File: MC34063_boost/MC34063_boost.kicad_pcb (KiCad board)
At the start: 2 copper layers, 88.6 x 24 mm, 24 parts, among them J1 INPUT, J2 OUTPUT, Q1 2N2222, U1 MC34063AP

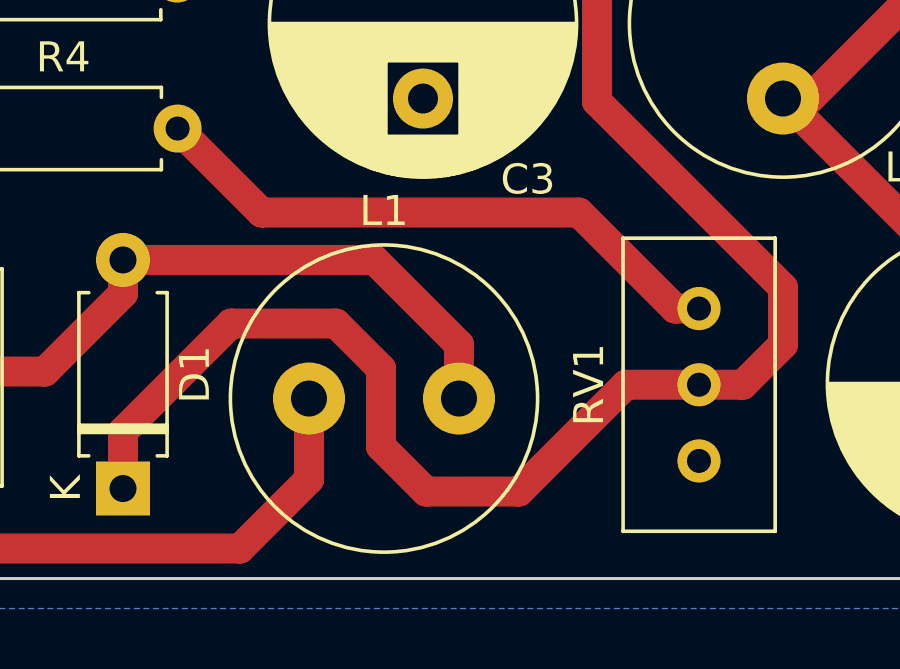
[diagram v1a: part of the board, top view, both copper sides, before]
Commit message: Made buck & inverter PCB's smaller for panelization
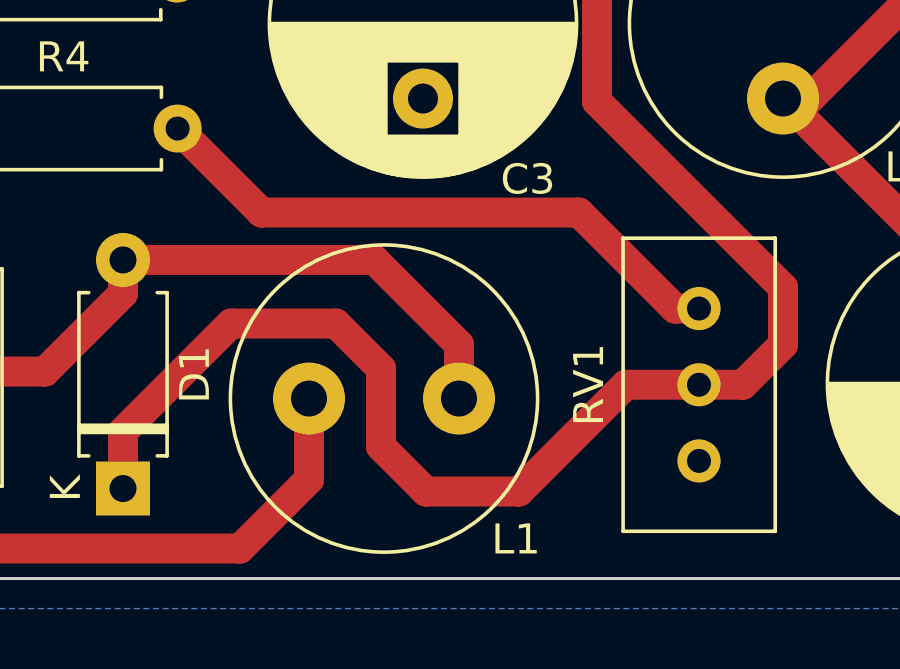
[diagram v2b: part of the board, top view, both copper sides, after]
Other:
- board text added: "https://github.com/DarioIriberri/MC34063_Converters"
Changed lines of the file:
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@@
   (general
     (thickness 1.6)
-    (drawings 13)
+    (drawings 14)
     (tracks 95)
     (zones 0)
@@
     (descr "Inductor, Radial series, Radial, pin pitch=5.00mm, , diameter=10.0mm, Neosid, SD12k, style3, http://www.neosid.de/produktblaetter/neosid_Festinduktivitaet_Sd12k.pdf")
     (tags "Inductor Radial series Radial pin pitch 5.00mm  diameter 10.0mm Neosid SD12k style3")
-    (fp_text reference L1 (at 2.5 -6.25) (layer F.SilkS)
+    (fp_text reference L1 (at 6.9 4.7) (layer F.SilkS)
       (effects (font (size 1 1) (thickness 0.15)))
     )
@@
     )
   )
+  (gr_text https://github.com/DarioIriberri/MC34063_Converters (at 104.1 81.5) (layer B.SilkS)
+    (effects (font (size 1.2 1.2) (thickness 0.15)) (justify mirror))
+  )
   (gr_text - (at 55.2 63.6 90) (layer F.SilkS)
     (effects (font (size 1.5 1.5) (thickness 0.3)))
@@
   (gr_line (start 45 83) (end 45 59) (layer Edge.Cuts) (width 0.1))
   (gr_line (start 133.6 83) (end 45 83) (layer Edge.Cuts) (width 0.1))
-  (segment (start 56.48 70.52) (end 59.98 70.52) (width 1) (layer F.Cu) (net 1))
   (segment (start 53.8 73.2) (end 56.48 70.52) (width 1) (layer F.Cu) (net 1))
   (segment (start 56.48 64.86) (end 58.34 63) (width 1) (layer F.Cu) (net 1))
@@
   (segment (start 52.5 68.7) (end 54.66 68.7) (width 1) (layer F.Cu) (net 1))
   (segment (start 53.5 73.5) (end 53.8 73.2) (width 1) (layer F.Cu) (net 1))
+  (segment (start 56.48 70.52) (end 59.98 70.52) (width 1) (layer F.Cu) (net 1))
   (segment (start 53.5 74.8) (end 53.5 73.5) (width 1) (layer F.Cu) (net 1))
-  (segment (start 71.3 77.7) (end 72.4 78.8) (width 1) (layer F.Cu) (net 3))
-  (segment (start 66.5 77.7) (end 71.3 77.7) (width 1) (layer F.Cu) (net 3))
+  (segment (start 67.6 70.52) (end 66.48 70.52) (width 1) (layer F.Cu) (net 3))
+  (segment (start 66.48 70.52) (end 65.3 71.7) (width 1) (layer F.Cu) (net 3))
   (segment (start 65.3 76.5) (end 66.5 77.7) (width 1) (layer F.Cu) (net 3))
   (segment (start 65.3 71.7) (end 65.3 76.5) (width 1) (layer F.Cu) (net 3))
-  (segment (start 66.48 70.52) (end 65.3 71.7) (width 1) (layer F.Cu) (net 3))
-  (segment (start 67.6 70.52) (end 66.48 70.52) (width 1) (layer F.Cu) (net 3))
+  (segment (start 66.5 77.7) (end 71.3 77.7) (width 1) (layer F.Cu) (net 3))
+  (segment (start 71.3 77.7) (end 72.4 78.8) (width 1) (layer F.Cu) (net 3))
   (segment (start 81.4 74.5) (end 84.9 74.5) (width 1) (layer F.Cu) (net 4))
   (segment (start 84.9 74.5) (end 86.4 76) (width 1) (layer F.Cu) (net 4))
@@
   (segment (start 122.7 74) (end 118 74) (width 1) (layer F.Cu) (net 7))
   (segment (start 125.8 70.9) (end 122.7 74) (width 1) (layer F.Cu) (net 7))
-  (segment (start 89 75.2) (end 89 77) (width 1) (layer F.Cu) (net 8) (status 20))
-  (segment (start 86.18 72.38) (end 89 75.2) (width 1) (layer F.Cu) (net 8))
-  (segment (start 77.8 72.38) (end 86.18 72.38) (width 1) (layer F.Cu) (net 8))
   (segment (start 67.6 75.6) (end 69.1 75.6) (width 1) (layer F.Cu) (net 8))
   (segment (start 69.1 75.6) (end 69.6 76.1) (width 1) (layer F.Cu) (net 8))
   (segment (start 69.6 76.1) (end 75.2 76.1) (width 1) (layer F.Cu) (net 8))
+  (segment (start 75.2 76.1) (end 77.8 73.5) (width 1) (layer F.Cu) (net 8))
   (segment (start 77.8 73.5) (end 77.8 72.38) (width 1) (layer F.Cu) (net 8))
-  (segment (start 75.2 76.1) (end 77.8 73.5) (width 1) (layer F.Cu) (net 8))
-  (segment (start 67.62 79.6) (end 67.8 79.6) (width 1) (layer F.Cu) (net 9) (status 30))
-  (segment (start 67.8 79.6) (end 70.2 82) (width 1) (layer F.Cu) (net 9) (status 10))
-  (segment (start 70.2 82) (end 81.7 82) (width 1) (layer F.Cu) (net 9))
-  (segment (start 84 79.7) (end 84 77) (width 1) (layer F.Cu) (net 9) (status 20))
-  (segment (start 81.7 82) (end 84 79.7) (width 1) (layer F.Cu) (net 9))
-  (segment (start 67.62 79.6) (end 64.5 79.6) (width 1) (layer F.Cu) (net 9))
-  (segment (start 64.5 79.6) (end 63 78.1) (width 1) (layer F.Cu) (net 9))
-  (segment (start 63 78.1) (end 63 74.7) (width 1) (layer F.Cu) (net 9))
-  (segment (start 61.36 73.06) (end 59.98 73.06) (width 1) (layer F.Cu) (net 9))
-  (segment (start 63 74.7) (end 61.36 73.06) (width 1) (layer F.Cu) (net 9))
+  (segment (start 77.8 72.38) (end 86.18 72.38) (width 1) (layer F.Cu) (net 8))
+  (segment (start 86.18 72.38) (end 89 75.2) (width 1) (layer F.Cu) (net 8))
+  (segment (start 89 75.2) (end 89 77) (width 1) (layer F.Cu) (net 8) (status 20))
   (segment (start 61.36 73.06) (end 61.36 72.94) (width 1) (layer F.Cu) (net 9))
   (segment (start 61.36 72.94) (end 63.1 71.2) (width 1) (layer F.Cu) (net 9))
@@
   (segment (start 67.6 63) (end 68.5 63) (width 1) (layer F.Cu) (net 9))
   (segment (start 63.1 67.5) (end 67.6 63) (width 1) (layer F.Cu) (net 9))
+  (segment (start 61.36 73.06) (end 59.98 73.06) (width 1) (layer F.Cu) (net 9))
+  (segment (start 67.62 79.6) (end 64.5 79.6) (width 1) (layer F.Cu) (net 9))
+  (segment (start 64.5 79.6) (end 63 78.1) (width 1) (layer F.Cu) (net 9))
+  (segment (start 63 78.1) (end 63 74.7) (width 1) (layer F.Cu) (net 9))
+  (segment (start 63 74.7) (end 61.36 73.06) (width 1) (layer F.Cu) (net 9))
+  (segment (start 67.62 79.6) (end 67.8 79.6) (width 1) (layer F.Cu) (net 9) (status 1000030))
+  (segment (start 67.8 79.6) (end 70.2 82) (width 1) (layer F.Cu) (net 9) (status 1000010))
+  (segment (start 70.2 82) (end 81.7 82) (width 1) (layer F.Cu) (net 9) (status 1000000))
+  (segment (start 84 79.7) (end 84 77) (width 1) (layer F.Cu) (net 9) (status 1000020))
+  (segment (start 81.7 82) (end 84 79.7) (width 1) (layer F.Cu) (net 9) (status 1000000))
   (segment (start 72 63.02) (end 71.98 63) (width 1) (layer F.Cu) (net 10))
   (segment (start 72 68) (end 72 63.02) (width 1) (layer F.Cu) (net 10))
@@
   (segment (start 71.98 62.48) (end 70 60.5) (width 1) (layer F.Cu) (net 10))
   (segment (start 70 60.5) (end 64.8 60.5) (width 1) (layer F.Cu) (net 10))
+  (segment (start 61.4 63.9) (end 61.4 66.56) (width 1) (layer F.Cu) (net 10))
   (segment (start 64.8 60.5) (end 61.4 63.9) (width 1) (layer F.Cu) (net 10))
   (segment (start 61.4 66.56) (end 59.98 67.98) (width 1) (layer F.Cu) (net 10))
-  (segment (start 61.4 63.9) (end 61.4 66.56) (width 1) (layer F.Cu) (net 10))
   (segment (start 60 75.62) (end 59.98 75.6) (width 1) (layer F.Cu) (net 11) (status 30))
   (segment (start 60 79.6) (end 60 75.62) (width 1) (layer F.Cu) (net 11) (status 30))
